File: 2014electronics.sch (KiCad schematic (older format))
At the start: 0 parts

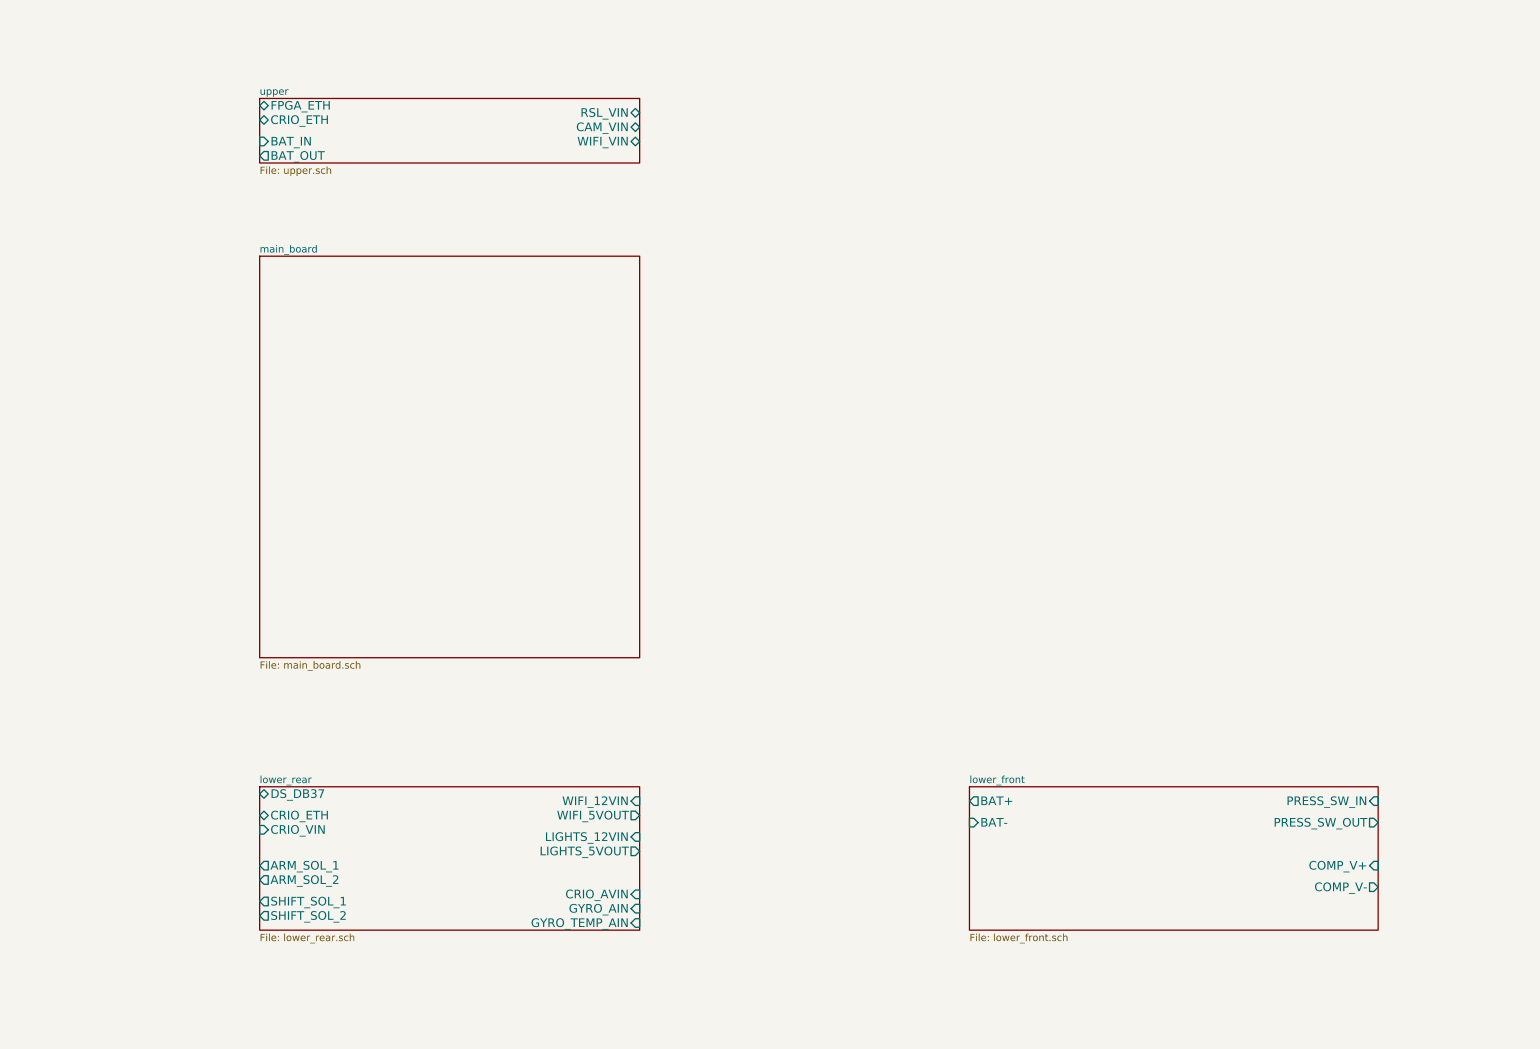
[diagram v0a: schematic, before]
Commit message: Udpates to main board and start of connector spec.
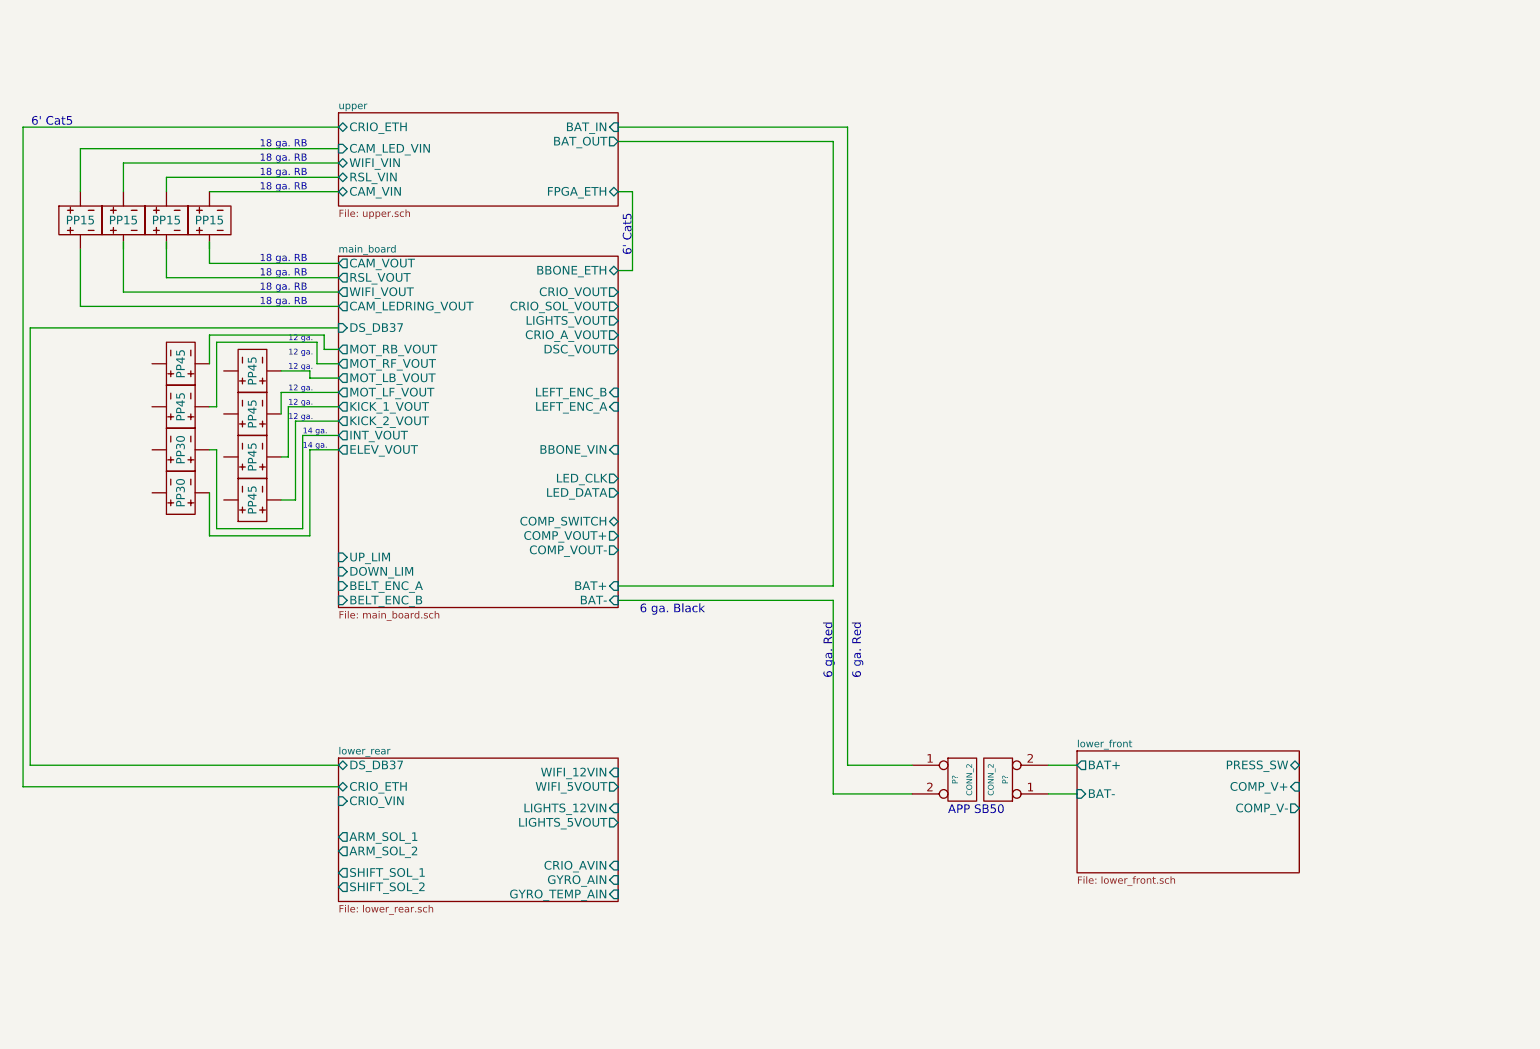
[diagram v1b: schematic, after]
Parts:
- added J? (x4): PP15, symbol PP15
- added J? (x6): PP45, symbol PP45
- added J? (x2): PP30, symbol PP30
- added P? (x2): CONN_2, symbol CONN_2
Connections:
- wire segments 0 -> 64
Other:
- note added: "12 ga."
- note added: "14 ga."
- note added: "18 ga. RB"
- note added: "6 ga. Black"
- note added: "6 ga. Red"
- note added: "6' Cat5"
- note added: "APP SB50"

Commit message: Cleaned up main board schematic a little more
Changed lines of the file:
@@
 F16 "KICK_2_VOUT" O L 2750 3450 60
 F17 "INT_VOUT" O L 2750 3550 60
-F18 "DSC_VOUT" O R 4700 2950 60
-F19 "BBONE_VIN" I R 4700 3650 60
-F20 "BBONE_ETH" B R 4700 2400 60
-F21 "LED_CLK" O R 4700 3850 60
-F22 "LED_DATA" O R 4700 3950 60
-F23 "UP_LIM" I L 2750 4400 60
-F24 "DOWN_LIM" I L 2750 4500 60
-F25 "RSL_VOUT" O L 2750 2450 60
-F26 "DS_DB37" I L 2750 2800 60
-F27 "LEFT_ENC_A" I R 4700 3350 60
-F28 "LEFT_ENC_B" I R 4700 3250 60
-F29 "COMP_SWITCH" B R 4700 4150 60
-F30 "BELT_ENC_A" I L 2750 4600 60
-F31 "BELT_ENC_B" I L 2750 4700 60
-F32 "CRIO_A_VOUT" O R 4700 2850 60
-F33 "COMP_VOUT+" O R 4700 4250 60
-F34 "COMP_VOUT-" O R 4700 4350 60
+F18 "BBONE_VIN" I R 4700 3650 60
+F19 "BBONE_ETH" B R 4700 2400 60
+F20 "LED_CLK" O R 4700 3850 60
+F21 "LED_DATA" O R 4700 3950 60
+F22 "UP_LIM" I L 2750 4400 60
+F23 "DOWN_LIM" I L 2750 4500 60
+F24 "RSL_VOUT" O L 2750 2450 60
+F25 "DS_DB37" I L 2750 2800 60
+F26 "LEFT_ENC_A" I R 4700 3350 60
+F27 "LEFT_ENC_B" I R 4700 3250 60
+F28 "COMP_SWITCH" B R 4700 4150 60
+F29 "BELT_ENC_A" I L 2750 4600 60
+F30 "BELT_ENC_B" I L 2750 4700 60
+F31 "CRIO_A_VOUT" O R 4700 2850 60
+F32 "COMP_VOUT+" O R 4700 4250 60
+F33 "COMP_VOUT-" O R 4700 4350 60
 $EndSheet
 $EndSCHEMATC

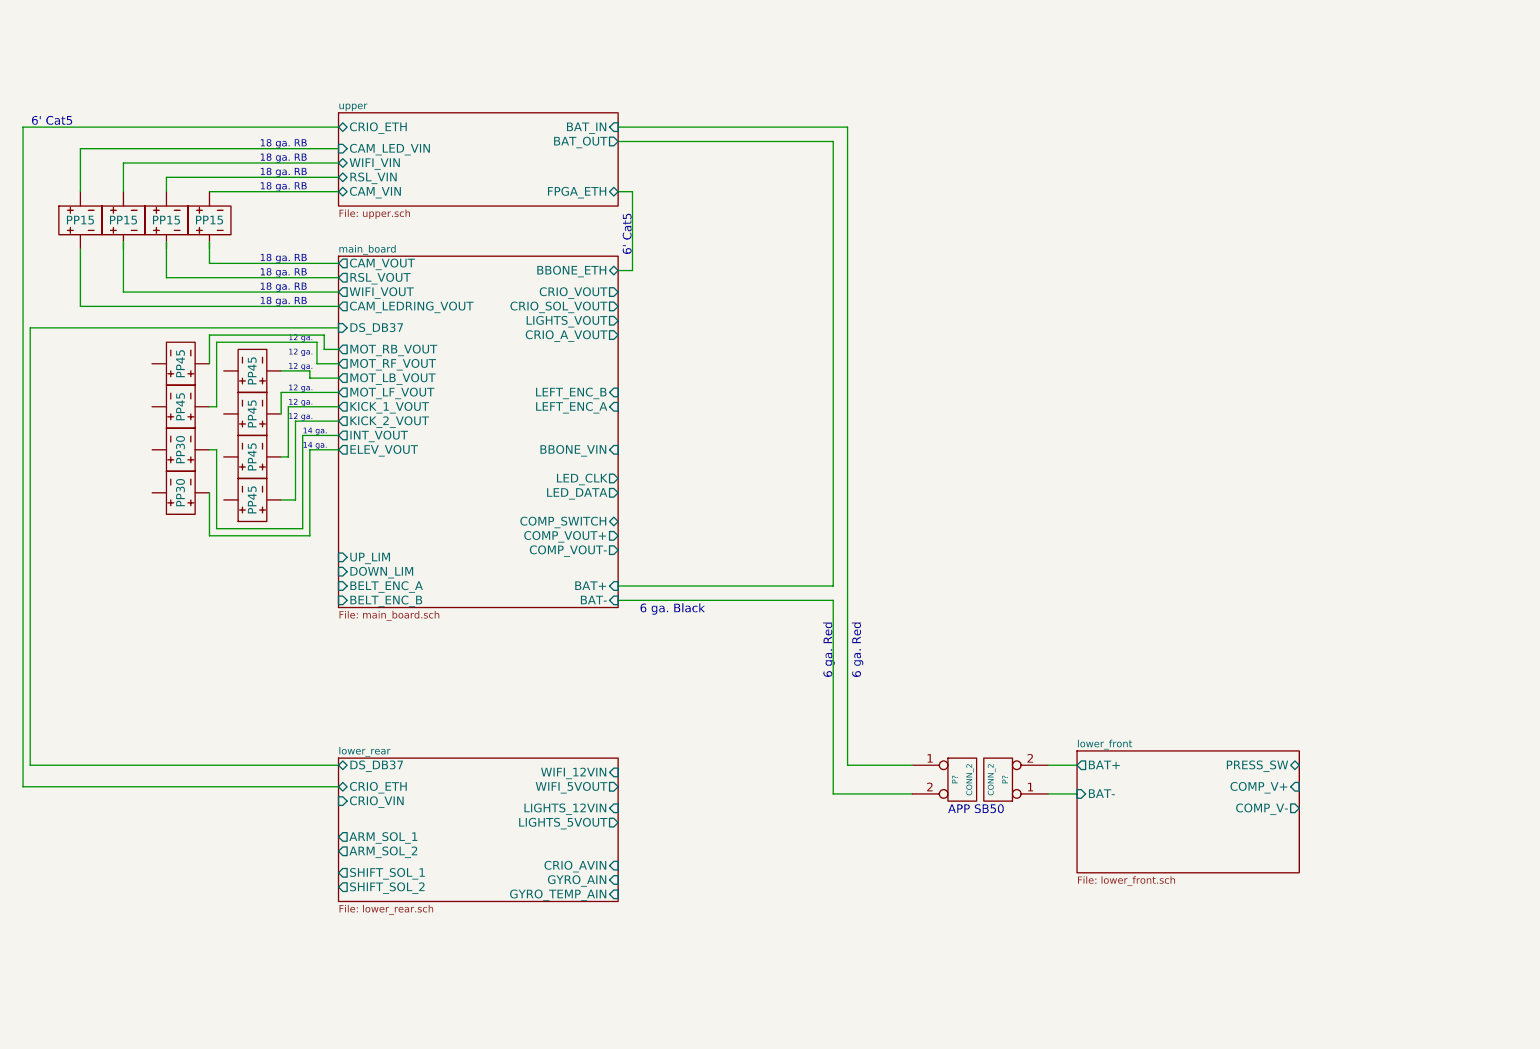
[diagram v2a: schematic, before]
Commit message: Added more connector blocks and wire sizes
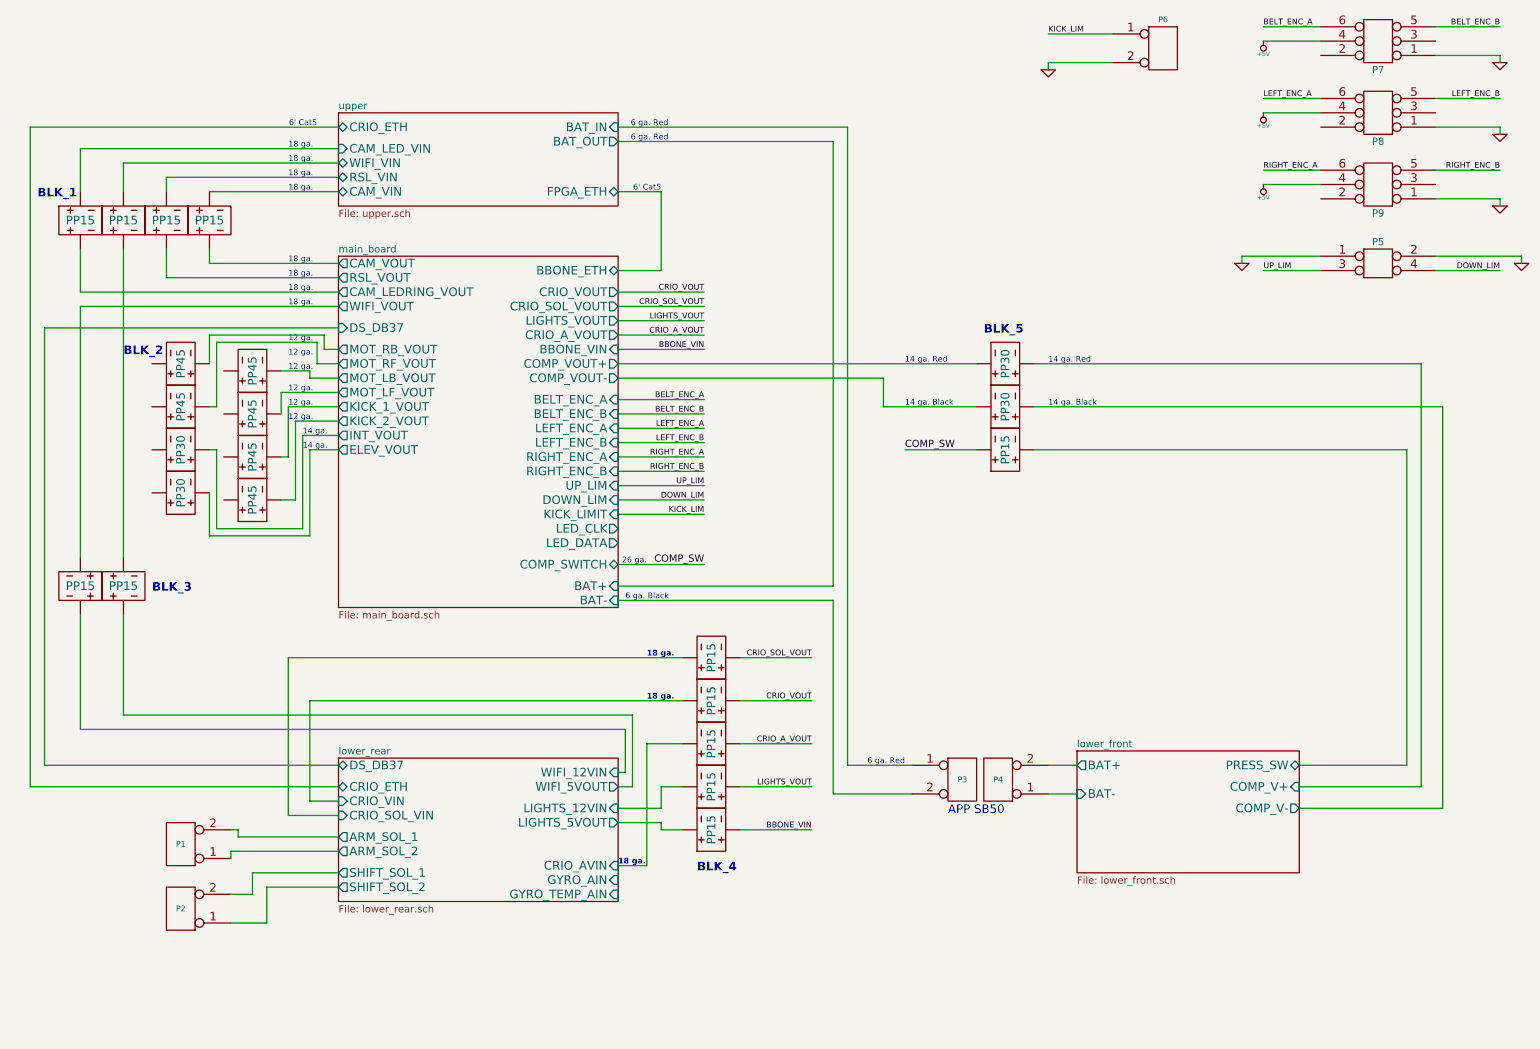
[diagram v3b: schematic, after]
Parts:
- added J15, J16, J17, J18, J19, J2, J22, J4: PP15, symbol PP15
- added J20, J21: PP30, symbol PP30
- added P1, P2, P6: CONN_2, symbol CONN_2
- added P5: CONN_2X2, symbol CONN_2X2
- added P7, P8, P9: CONN_3X2, symbol CONN_3X2
- gave numbers to parts that had none: 14
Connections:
- net labels added: +5V, BBONE_VIN, BELT_ENC_A, BELT_ENC_B, COMP_SW, CRIO_A_VOUT, CRIO_SOL_VOUT, CRIO_VOUT, DOWN_LIM, GND, KICK_LIM, LEFT_ENC_A, LEFT_ENC_B, LIGHTS_VOUT, RIGHT_ENC_A, RIGHT_ENC_B, UP_LIM
- wire segments 64 -> 157
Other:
- note added: "14 ga. Black"
- note added: "14 ga. Red"
- note added: "18 ga."
- note added: "26 ga."
- note added: "BLK_1"
- note added: "BLK_2"
- note added: "BLK_3"
- note added: "BLK_4"
- note added: "BLK_5"
- note removed: "18 ga. RB"

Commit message: Added more wire size annotations.  Added labels for motor block.
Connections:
- net main_board/COMP_VOUT+ is gone; now on net lower_front/COMP_V-: J20.~
- net main_board/COMP_VOUT- is gone; now on net lower_front/COMP_V+: J21.~
- net main_board/ELEV_VOUT is gone; now on net ELEV_VOUT: J9.~
- net main_board/INT_VOUT is gone; now on net INT_VOUT: J8.~
- net main_board/KICK_1_VOUT is gone; now on net MOT_LB_VOUT: J13.~
- net main_board/KICK_2_VOUT is gone; now on net MOT_LF_VOUT: J14.~
- net main_board/MOT_LB_VOUT is gone; now on net MOT_RB_VOUT: J11.~
- net main_board/MOT_LF_VOUT is gone; now on net MOT_RF_VOUT: J12.~
- net main_board/MOT_RB_VOUT is gone; now on net KICK_1_VOUT: J6.~
- net main_board/MOT_RF_VOUT is gone; now on net KICK_2_VOUT: J7.~
- net lower_front/COMP_V+: no longer J20.~
- net lower_front/COMP_V-: no longer J21.~
- net MOT_RB_VOUT: now reaches J11.~
- net MOT_RF_VOUT: now reaches J12.~
- net KICK_1_VOUT: now reaches J6.~
- net KICK_2_VOUT: now reaches J7.~
- net MOT_LF_VOUT: now reaches J14.~
- net MOT_LB_VOUT: now reaches J13.~
- net INT_VOUT: now reaches J8.~
- net ELEV_VOUT: now reaches J9.~
- new net: J3.~, J4.~
- new net COMP_VOUT+: J21.~
- new net COMP_VOUT-: J20.~
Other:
- note added: "6 ga."
- note removed: "6' Cat5"
- moved on the sheet: P1, P2
